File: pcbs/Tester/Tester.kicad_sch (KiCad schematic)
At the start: 0 parts

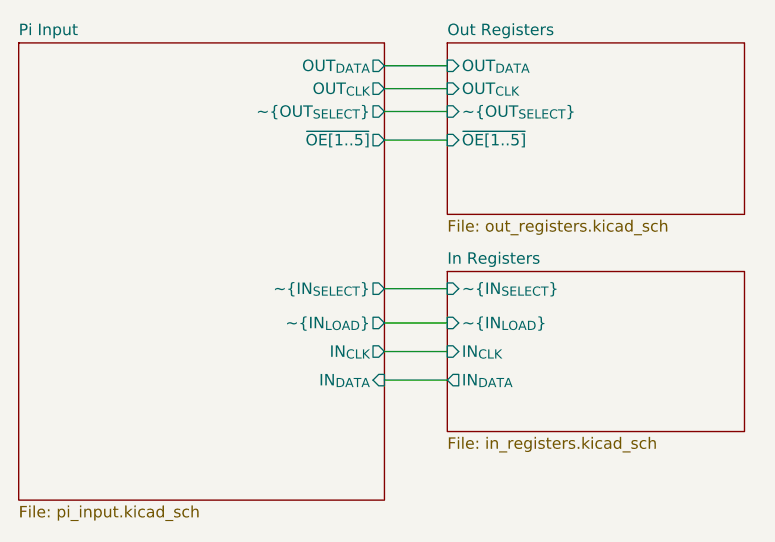
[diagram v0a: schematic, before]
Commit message: Fix Tester board (#49)
The 'input' level shifter on the Tester board had the wrong set of pins connected to ground (copy paste error from the 'output' level shifters). This meant that the IC could effectively short circuit and become very hot. Switch over the ground and floating pins, to reflect how the inputs and outputs are for this IC.

Closes #47
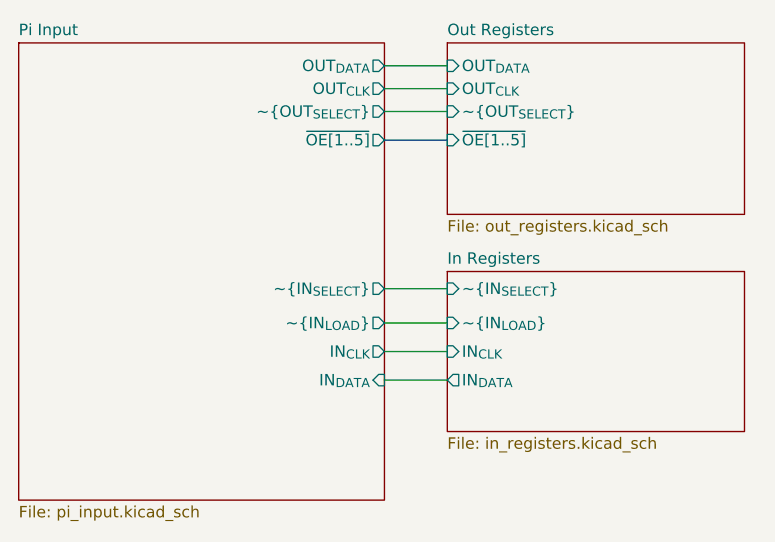
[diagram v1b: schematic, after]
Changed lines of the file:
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@@
-    (stroke (width 0) (type default) (color 0 0 0 0))
-  )
-  (wire (pts (xy 69.215 55.245) (xy 76.2 55.245))
     (stroke (width 0) (type default) (color 0 0 0 0))
   )
@@
     (stroke (width 0) (type default) (color 0 0 0 0))
   )
+  (bus (pts (xy 69.215 55.245) (xy 76.2 55.245))
+    (stroke (width 0) (type default) (color 0 0 0 0))
+  )
